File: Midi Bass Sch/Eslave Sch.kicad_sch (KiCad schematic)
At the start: 12 parts, among them J3 E SLAVE ISCP, SW3 E-slave Reset

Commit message: added footprints to kicad schematic still need footprint for din connector
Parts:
- C2: footprint (none) -> Capacitor_SMD:C_0805_2012Metric_Pad1.18x1.45mm_HandSolder
- D10, D8, D9: footprint (none) -> Diode_SMD:D_0805_2012Metric_Pad1.15x1.40mm_HandSolder
- J3: footprint (none) -> Connector_PinHeader_2.54mm:PinHeader_1x06_P2.54mm_Vertical
- R15, R16, R17, R18: footprint (none) -> Resistor_SMD:R_0805_2012Metric_Pad1.20x1.40mm_HandSolder
- U2: value ~ -> PIC16F1789
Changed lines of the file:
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@@
 			)
 		)
-		(property "Footprint" ""
+		(property "Footprint" "Diode_SMD:D_0805_2012Metric_Pad1.15x1.40mm_HandSolder"
 			(at 201.93 120.65 0)
 			(effects
@@
 			)
 		)
-		(property "Footprint" ""
+		(property "Footprint" "Resistor_SMD:R_0805_2012Metric_Pad1.20x1.40mm_HandSolder"
 			(at 57.15 127 0)
 			(effects
@@
 			)
 		)
-		(property "Footprint" ""
+		(property "Footprint" "Capacitor_SMD:C_0805_2012Metric_Pad1.18x1.45mm_HandSolder"
 			(at 59.69 130.81 0)
 			(effects
@@
 			)
 		)
-		(property "Footprint" ""
+		(property "Footprint" "Connector_PinHeader_2.54mm:PinHeader_1x06_P2.54mm_Vertical"
 			(at 25.4 48.26 0)
 			(effects
@@
 			)
 		)
-		(property "Footprint" ""
+		(property "Footprint" "Resistor_SMD:R_0805_2012Metric_Pad1.20x1.40mm_HandSolder"
 			(at 35.56 138.43 0)
 			(effects
@@
 			)
 		)
-		(property "Footprint" ""
+		(property "Footprint" "Resistor_SMD:R_0805_2012Metric_Pad1.20x1.40mm_HandSolder"
 			(at 185.42 114.3 0)
 			(effects
@@
 			)
 		)
-		(property "Value" "~"
-			(at 131.7341 153.67 0)
+		(property "Value" "PIC16F1789"
+			(at 126.238 28.194 0)
 			(effects
 				(font
@@
 			)
 		)
-		(property "Footprint" ""
+		(property "Footprint" "Resistor_SMD:R_0805_2012Metric_Pad1.20x1.40mm_HandSolder"
 			(at 199.39 111.76 0)
 			(effects
@@
 			)
 		)
-		(property "Footprint" ""
+		(property "Footprint" "Diode_SMD:D_0805_2012Metric_Pad1.15x1.40mm_HandSolder"
 			(at 68.58 132.08 0)
 			(effects
@@
 			)
 		)
-		(property "Footprint" ""
+		(property "Footprint" "Diode_SMD:D_0805_2012Metric_Pad1.15x1.40mm_HandSolder"
 			(at 187.96 123.19 0)
 			(effects

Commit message: started basic pcb layout for Master pic
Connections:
- net MSCLR E: now also D8.1; no longer D8.2
- net at C2.1, R16.1, SW3.2: now also D8.2; no longer D8.1

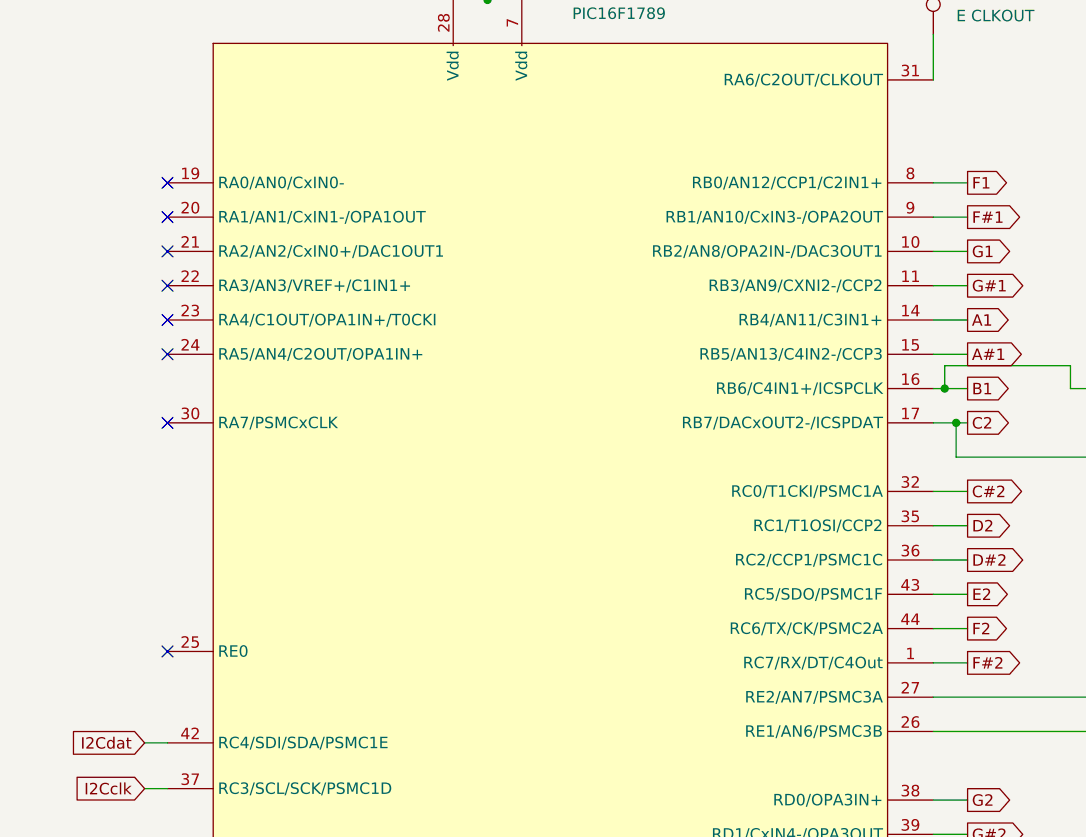
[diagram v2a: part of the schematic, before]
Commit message: updated schematic to reflect code
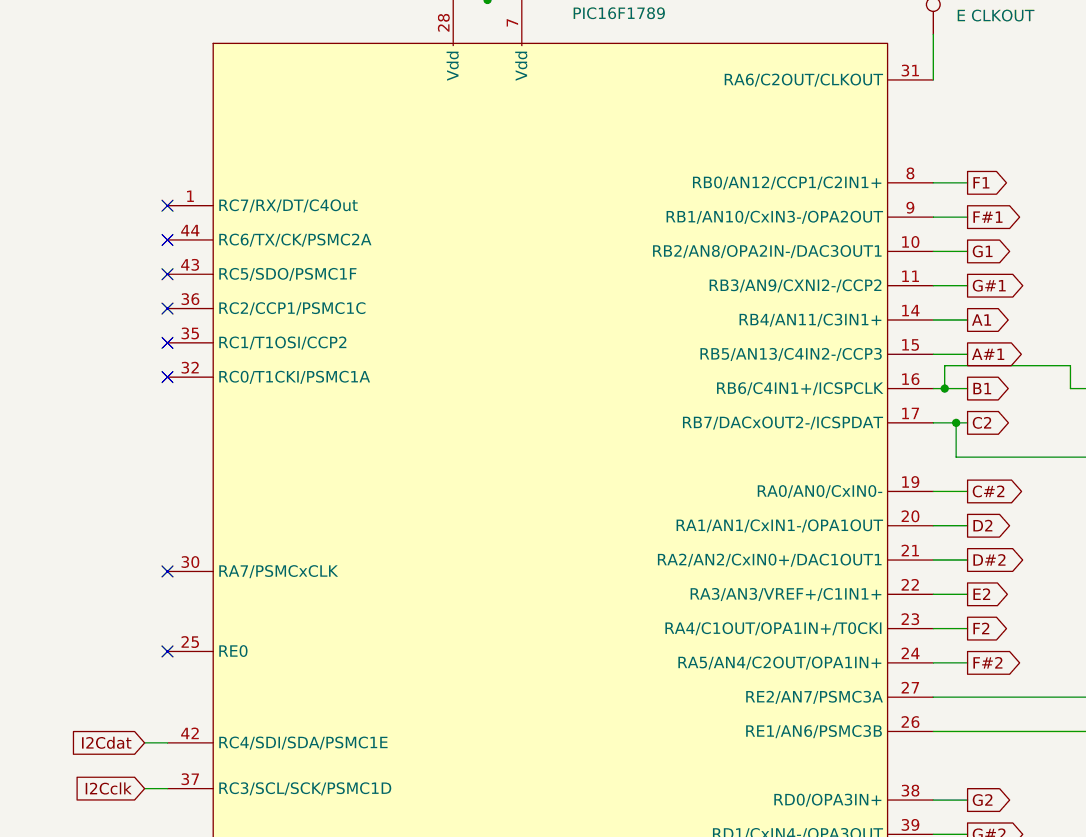
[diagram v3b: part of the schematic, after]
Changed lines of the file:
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@@
 	)
 	(no_connect
-		(at 81.28 46.99)
+		(at 81.28 49.53)
 	)
 	(no_connect
-		(at 81.28 58.42)
+		(at 81.28 60.96)
 	)
 	(no_connect
-		(at 81.28 66.04)
+		(at 81.28 68.58)
 	)
 	(no_connect
-		(at 81.28 50.8)
+		(at 81.28 90.17)
+	)
+	(no_connect
+		(at 81.28 53.34)
 	)
 	(no_connect
@@
 	)
 	(no_connect
-		(at 81.28 62.23)
+		(at 81.28 64.77)
 	)
 	(no_connect
@@
 	)
 	(no_connect
-		(at 81.28 54.61)
+		(at 81.28 57.15)
 	)
 	(no_connect
 		(at 166.37 138.43)
 	)
-	(no_connect
-		(at 81.28 73.66)
-	)
 	(wire

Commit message: finished troubleshooting section
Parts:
- added J4: E Slave Out, symbol Owen's Symbols:Header_1x21
- added J5: Solenoid In, symbol Owen's Symbols:Header_1x21
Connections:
- net A#1: now also J4.6, J5.6
- net A#2: now also J4.18, J5.18
- net A1: now also J4.5, J5.5
- net A2: now also J4.17, J5.17
- net B1: now also J4.7, J5.7
- net B2: now also J4.19, J5.19
- net C#2: now also J4.9, J5.9
- net C2: now also J4.8, J5.8
- net C3: now also J4.20, J5.20
- net D#2: now also J4.11, J5.11
- net D2: now also J4.10, J5.10
- net E2: now also J4.12, J5.12
- net F#1: now also J4.2, J5.2
- net F#2: now also J4.14, J5.14
- net F1: now also J4.1, J5.1
- net F2: now also J4.13, J5.13
- net G#1: now also J4.4, J5.4
- net G#2: now also J4.16, J5.16
- net G1: now also J4.3, J5.3
- net G2: now also J4.15, J5.15
- net GND: now also J4.21, J5.21
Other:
- moved on the sheet: D10, D9, R17, R18

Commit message: began getting images for schematic appendix
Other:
- title: (none) -> E-Slave Processor Schematic
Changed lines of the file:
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@@
 	(generator_version "8.0")
 	(paper "A")
+	(title_block
+		(title "E-Slave Processor Schematic")
+		(date "2024-12-10")
+		(rev "A")
+	)
 	(junction
 		(at 59.69 130.81)

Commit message: began working on pcb layout deleted extra schematics for solenoid break out board
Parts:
- J4, J5: footprint (none) -> Connector_PinHeader_2.54mm:PinHeader_1x21_P2.54mm_Vertical
- SW3: footprint (none) -> Button_Switch_THT:SW_PUSH_6mm_H5mm
- TP5: footprint (none) -> Connector_PinHeader_2.54mm:PinHeader_1x01_P2.54mm_Vertical
- U2: footprint (none) -> OF footprints:TQFN-44_7x7_Pitch0.4mm
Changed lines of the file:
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@@
 			)
 		)
-		(property "Footprint" ""
+		(property "Footprint" "Connector_PinHeader_2.54mm:PinHeader_1x01_P2.54mm_Vertical"
 			(at 171.45 30.48 0)
 			(effects
@@
 			)
 		)
-		(property "Footprint" ""
+		(property "Footprint" "Connector_PinHeader_2.54mm:PinHeader_1x21_P2.54mm_Vertical"
 			(at 201.93 43.18 0)
 			(effects
@@
 			)
 		)
-		(property "Footprint" ""
+		(property "Footprint" "Button_Switch_THT:SW_PUSH_6mm_H5mm"
 			(at 49.53 125.73 0)
 			(effects
@@
 			)
 		)
-		(property "Footprint" ""
+		(property "Footprint" "OF footprints:TQFN-44_7x7_Pitch0.4mm"
 			(at 90.17 41.91 0)
 			(effects
@@
 			)
 		)
-		(property "Footprint" ""
+		(property "Footprint" "Connector_PinHeader_2.54mm:PinHeader_1x21_P2.54mm_Vertical"
 			(at 217.17 43.18 0)
 			(effects
